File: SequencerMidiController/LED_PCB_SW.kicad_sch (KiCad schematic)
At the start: 1 part, among them U32 PCB-SPST_RGB-LED-Counter-Cloc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

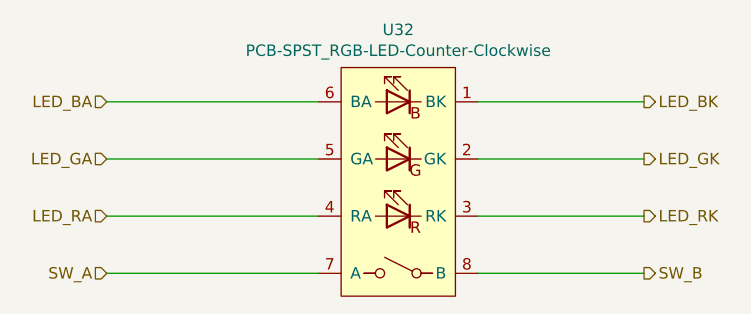
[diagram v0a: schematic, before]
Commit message: updated user buttons
removed dipsw, added four more tactile button (three above display, three below display, six total)
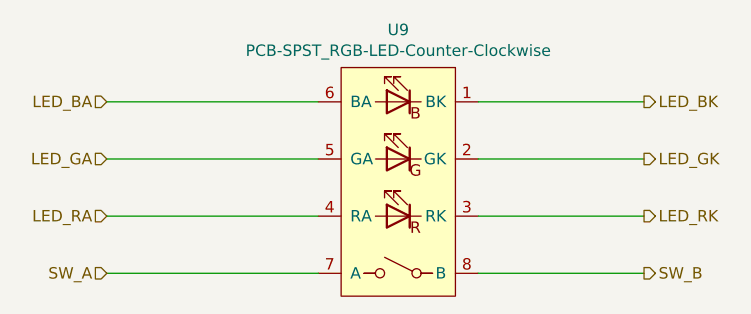
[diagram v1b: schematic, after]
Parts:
- renumbered U32 to U9
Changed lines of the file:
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@@
   (symbol (lib_id "PCB_LED_SW:PCB-SPST_RGB-LED-Counter-Clockwise") (at 158.115 97.79 0) (mirror y)
     (in_bom yes) (on_board yes)
-    (property "Reference" "U32" (id 0) (at 158.115 80.899 0))
+    (property "Reference" "U9" (id 0) (at 158.115 80.899 0))
     (property "Value" "PCB-SPST_RGB-LED-Counter-Clockwise" (id 1) (at 158.115 83.2104 0))
     (property "Footprint" "PCB_SW_LED:Circular_3mm_10mm_Cree_PLLC6_CLY6D-FKC-CK1N1D1BB7D3D3" (id 2) (at 158.115 82.55 0)
